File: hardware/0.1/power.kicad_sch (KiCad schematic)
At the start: 31 parts, among them U1 ECP5U_12_CABGA256, U2 TLV73325PDBV, U3 TLV62568DBV, U5 TLV62568DBV

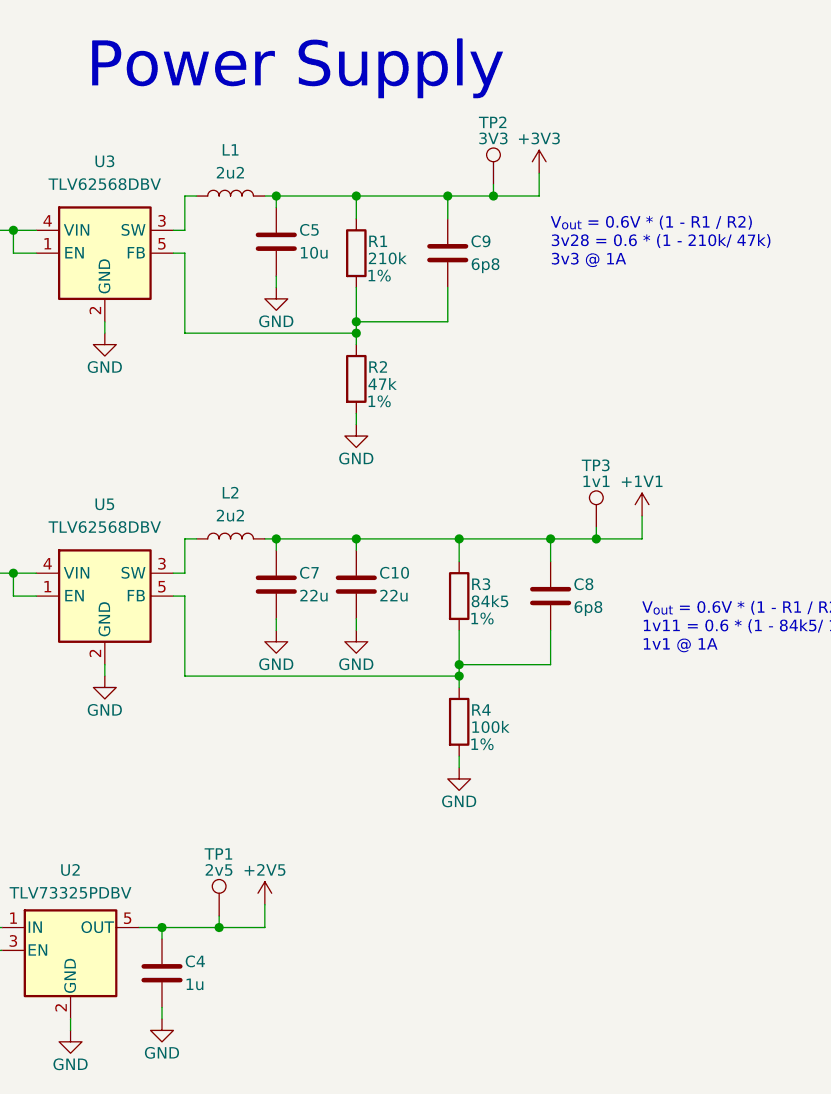
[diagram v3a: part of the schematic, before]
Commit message: hyperram routed
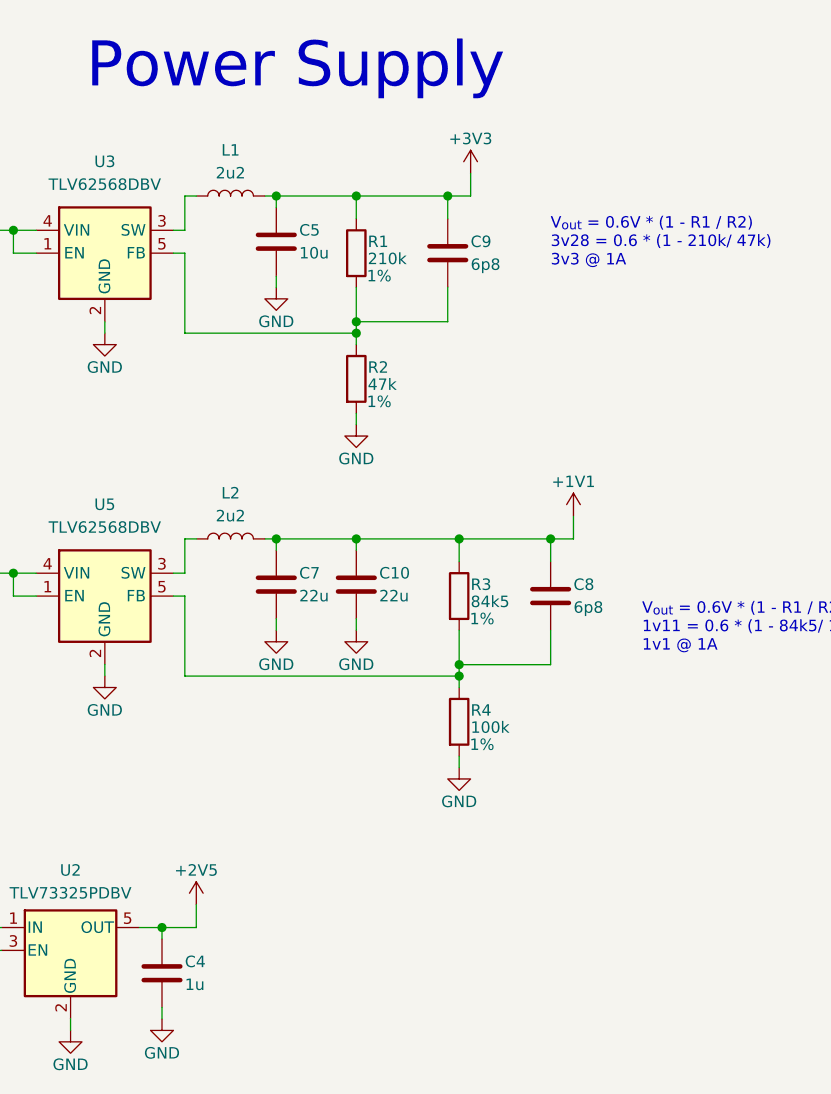
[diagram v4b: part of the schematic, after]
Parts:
- removed TP1: 2v5, TestPoint:TestPoint_Pad_D1.5mm, symbol Connector:TestPoint
- removed TP2: 3V3, TestPoint:TestPoint_Pad_D1.5mm, symbol Connector:TestPoint
- removed TP3: 1v1, TestPoint:TestPoint_Pad_D1.5mm, symbol Connector:TestPoint
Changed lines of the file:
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@@
   (junction (at 34.29 81.28) (diameter 1.016) (color 0 0 0 0))
   (junction (at 50.8 120.65) (diameter 1.016) (color 0 0 0 0))
-  (junction (at 57.15 120.65) (diameter 1.016) (color 0 0 0 0))
   (junction (at 63.5 39.37) (diameter 1.016) (color 0 0 0 0))
   (junction (at 63.5 77.47) (diameter 1.016) (color 0 0 0 0))
@@
   (junction (at 83.82 91.44) (diameter 1.016) (color 0 0 0 0))
   (junction (at 83.82 92.71) (diameter 1.016) (color 0 0 0 0))
-  (junction (at 87.63 39.37) (diameter 1.016) (color 0 0 0 0))
   (junction (at 93.98 77.47) (diameter 1.016) (color 0 0 0 0))
-  (junction (at 99.06 77.47) (diameter 1.016) (color 0 0 0 0))
   (junction (at 182.88 76.2) (diameter 1.016) (color 0 0 0 0))
   (junction (at 182.88 86.36) (diameter 1.016) (color 0 0 0 0))
@@
     (stroke (width 0) (type solid) (color 0 0 0 0))
   )
-  (wire (pts (xy 50.8 120.65) (xy 57.15 120.65))
+  (wire (pts (xy 50.8 120.65) (xy 54.61 120.65))
     (stroke (width 0) (type solid) (color 0 0 0 0))
   )
@@
     (stroke (width 0) (type solid) (color 0 0 0 0))
   )
-  (wire (pts (xy 57.15 119.38) (xy 57.15 120.65))
-    (stroke (width 0) (type solid) (color 0 0 0 0))
-  )
-  (wire (pts (xy 57.15 120.65) (xy 62.23 120.65))
+  (wire (pts (xy 54.61 118.11) (xy 54.61 120.65))
     (stroke (width 0) (type solid) (color 0 0 0 0))
   )
@@
     (stroke (width 0) (type solid) (color 0 0 0 0))
   )
-  (wire (pts (xy 62.23 118.11) (xy 62.23 120.65))
-    (stroke (width 0) (type solid) (color 0 0 0 0))
-  )
   (wire (pts (xy 63.5 39.37) (xy 63.5 40.64))
     (stroke (width 0) (type solid) (color 0 0 0 0))
@@
     (stroke (width 0) (type solid) (color 0 0 0 0))
   )
-  (wire (pts (xy 82.55 39.37) (xy 87.63 39.37))
+  (wire (pts (xy 82.55 39.37) (xy 85.09 39.37))
     (stroke (width 0) (type solid) (color 0 0 0 0))
   )
@@
     (stroke (width 0) (type solid) (color 0 0 0 0))
   )
-  (wire (pts (xy 87.63 38.1) (xy 87.63 39.37))
-    (stroke (width 0) (type solid) (color 0 0 0 0))
-  )
-  (wire (pts (xy 87.63 39.37) (xy 92.71 39.37))
-    (stroke (width 0) (type solid) (color 0 0 0 0))
-  )
-  (wire (pts (xy 92.71 39.37) (xy 92.71 36.83))
+  (wire (pts (xy 85.09 39.37) (xy 85.09 36.83))
     (stroke (width 0) (type solid) (color 0 0 0 0))
   )
@@
     (stroke (width 0) (type solid) (color 0 0 0 0))
   )
-  (wire (pts (xy 93.98 77.47) (xy 99.06 77.47))
+  (wire (pts (xy 93.98 77.47) (xy 96.52 77.47))
     (stroke (width 0) (type solid) (color 0 0 0 0))
   )
@@
     (stroke (width 0) (type solid) (color 0 0 0 0))
   )
-  (wire (pts (xy 99.06 76.2) (xy 99.06 77.47))
-    (stroke (width 0) (type solid) (color 0 0 0 0))
-  )
-  (wire (pts (xy 99.06 77.47) (xy 104.14 77.47))
-    (stroke (width 0) (type solid) (color 0 0 0 0))
-  )
-  (wire (pts (xy 104.14 77.47) (xy 104.14 74.93))
+  (wire (pts (xy 96.52 77.47) (xy 96.52 74.93))
     (stroke (width 0) (type solid) (color 0 0 0 0))
   )
@@
     (effects (font (size 5 5)) (justify right bottom))
   )
-  (symbol (lib_id "Connector:TestPoint") (at 57.15 119.38 0) (unit 1)
-    (in_bom yes) (on_board yes)
-    (property "Reference" "TP1" (id 0) (at 57.15 112.522 0))
-    (property "Value" "2v5" (id 1) (at 57.15 114.3 0))
-    (property "Footprint" "TestPoint:TestPoint_Pad_D1.5mm" (id 2) (at 62.23 119.38 0)
-      (effects (font (size 1.27 1.27)) hide)
-    )
-    (property "Datasheet" "~" (id 3) (at 62.23 119.38 0)
-      (effects (font (size 1.27 1.27)) hide)
-    )
-  )
-  (symbol (lib_id "Connector:TestPoint") (at 87.63 38.1 0) (unit 1)
-    (in_bom yes) (on_board yes)
-    (property "Reference" "TP2" (id 0) (at 87.63 31.242 0))
-    (property "Value" "3V3" (id 1) (at 87.63 33.02 0))
-    (property "Footprint" "TestPoint:TestPoint_Pad_D1.5mm" (id 2) (at 92.71 38.1 0)
-      (effects (font (size 1.27 1.27)) hide)
-    )
-    (property "Datasheet" "~" (id 3) (at 92.71 38.1 0)
-      (effects (font (size 1.27 1.27)) hide)
-    )
-  )
-  (symbol (lib_id "Connector:TestPoint") (at 99.06 76.2 0) (unit 1)
-    (in_bom yes) (on_board yes)
-    (property "Reference" "TP3" (id 0) (at 99.06 69.342 0))
-    (property "Value" "1v1" (id 1) (at 99.06 71.12 0))
-    (property "Footprint" "TestPoint:TestPoint_Pad_D1.5mm" (id 2) (at 104.14 76.2 0)
-      (effects (font (size 1.27 1.27)) hide)
-    )
-    (property "Datasheet" "~" (id 3) (at 104.14 76.2 0)
-      (effects (font (size 1.27 1.27)) hide)
-    )
-  )
   (symbol (lib_id "power:+5V") (at 24.13 118.745 0) (unit 1)
     (in_bom yes) (on_board yes)
@@
     )
   )
-  (symbol (lib_id "power:+2V5") (at 62.23 118.11 0) (unit 1)
-    (in_bom yes) (on_board yes)
-    (property "Reference" "#PWR0112" (id 0) (at 62.23 121.92 0)
-      (effects (font (size 1.27 1.27)) hide)
-    )
-    (property "Value" "+2V5" (id 1) (at 62.23 114.3 0))
-    (property "Footprint" "" (id 2) (at 62.23 118.11 0)
-      (effects (font (size 1.27 1.27)) hide)
-    )
-    (property "Datasheet" "" (id 3) (at 62.23 118.11 0)
-      (effects (font (size 1.27 1.27)) hide)
-    )
-  )
-  (symbol (lib_id "power:+3V3") (at 92.71 36.83 0) (unit 1)
-    (in_bom yes) (on_board yes)
-    (property "Reference" "#PWR0101" (id 0) (at 92.71 40.64 0)
-      (effects (font (size 1.27 1.27)) hide)
-    )
-    (property "Value" "+3V3" (id 1) (at 92.71 33.02 0))
-    (property "Footprint" "" (id 2) (at 92.71 36.83 0)
-      (effects (font (size 1.27 1.27)) hide)
-    )
-    (property "Datasheet" "" (id 3) (at 92.71 36.83 0)
-      (effects (font (size 1.27 1.27)) hide)
-    )
-  )
-  (symbol (lib_id "power:+1V1") (at 104.14 74.93 0) (unit 1)
-    (in_bom yes) (on_board yes)
-    (property "Reference" "#PWR0107" (id 0) (at 104.14 78.74 0)
-      (effects (font (size 1.27 1.27)) hide)
-    )
-    (property "Value" "+1V1" (id 1) (at 104.14 71.12 0))
-    (property "Footprint" "" (id 2) (at 104.14 74.93 0)
-      (effects (font (size 1.27 1.27)) hide)
-    )
-    (property "Datasheet" "" (id 3) (at 104.14 74.93 0)
-      (effects (font (size 1.27 1.27)) hide)
-    )
+  (symbol (lib_id "power:+2V5") (at 54.61 118.11 0) (unit 1)
+    (in_bom yes) (on_board yes)
+    (property "Reference" "#PWR0112" (id 0) (at 54.61 121.92 0)
+      (effects (font (size 1.27 1.27)) hide)
+    )
+    (property "Value" "+2V5" (id 1) (at 54.61 114.3 0))
+    (property "Footprint" "" (id 2) (at 54.61 118.11 0)
+      (effects (font (size 1.27 1.27)) hide)
+    )
+    (property "Datasheet" "" (id 3) (at 54.61 118.11 0)
+      (effects (font (size 1.27 1.27)) hide)
+    )
+  )
+  (symbol (lib_id "power:+3V3") (at 85.09 36.83 0) (unit 1)
+    (in_bom yes) (on_board yes)
+    (property "Reference" "#PWR0101" (id 0) (at 85.09 40.64 0)
+      (effects (font (size 1.27 1.27)) hide)
+    )
+    (property "Value" "+3V3" (id 1) (at 85.09 33.02 0))
+    (property "Footprint" "" (id 2) (at 85.09 36.83 0)
+      (effects (font (size 1.27 1.27)) hide)
+    )
+    (property "Datasheet" "" (id 3) (at 85.09 36.83 0)
+      (effects (font (size 1.27 1.27)) hide)
+    )
+  )
+  (symbol (lib_id "power:+1V1") (at 96.52 74.93 0) (unit 1)
+    (in_bom yes) (on_board yes)
+    (property "Reference" "#PWR0107" (id 0) (at 96.52 78.74 0)
+      (effects (font (size 1.27 1.27)) hide)
+    )
+    (property "Value" "+1V1" (id 1) (at 96.52 71.12 0))
+    (property "Footprint" "" (id 2) (at 96.52 74.93 0)
+      (effects (font (size 1.27 1.27)) hide)
+    )
+    (property "Datasheet" "" (id 3) (at 96.52 74.93 0)
+      (effects (font (size 1.27 1.27)) hide)
+    )

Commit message: all DRC / ERC errors signed off
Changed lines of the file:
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@@
+    (stroke (width 0) (type solid) (color 0 0 0 0))
+  )
+  (wire (pts (xy 142.24 189.23) (xy 142.24 190.5))
+    (stroke (width 0) (type solid) (color 0 0 0 0))
+  )
+  (wire (pts (xy 151.13 190.5) (xy 151.13 189.23))
+    (stroke (width 0) (type solid) (color 0 0 0 0))
+  )
+  (wire (pts (xy 161.29 190.5) (xy 161.29 189.23))
+    (stroke (width 0) (type solid) (color 0 0 0 0))
+  )
+  (wire (pts (xy 171.45 190.5) (xy 171.45 189.23))
     (stroke (width 0) (type solid) (color 0 0 0 0))
   )
@@
     (effects (font (size 5 5)) (justify right bottom))
   )
+  (symbol (lib_id "power:PWR_FLAG") (at 142.24 189.23 0) (unit 1)
+    (in_bom yes) (on_board yes)
+    (property "Reference" "#FLG0102" (id 0) (at 142.24 187.325 0)
+      (effects (font (size 1.27 1.27)) hide)
+    )
+    (property "Value" "PWR_FLAG" (id 1) (at 142.24 185.42 0))
+    (property "Footprint" "" (id 2) (at 142.24 189.23 0)
+      (effects (font (size 1.27 1.27)) hide)
+    )
+    (property "Datasheet" "~" (id 3) (at 142.24 189.23 0)
+      (effects (font (size 1.27 1.27)) hide)
+    )
+  )
+  (symbol (lib_id "power:PWR_FLAG") (at 151.13 190.5 180) (unit 1)
+    (in_bom yes) (on_board yes)
+    (property "Reference" "#FLG0104" (id 0) (at 151.13 192.405 0)
+      (effects (font (size 1.27 1.27)) hide)
+    )
+    (property "Value" "PWR_FLAG" (id 1) (at 151.13 194.31 0))
+    (property "Footprint" "" (id 2) (at 151.13 190.5 0)
+      (effects (font (size 1.27 1.27)) hide)
+    )
+    (property "Datasheet" "~" (id 3) (at 151.13 190.5 0)
+      (effects (font (size 1.27 1.27)) hide)
+    )
+  )
+  (symbol (lib_id "power:PWR_FLAG") (at 161.29 190.5 180) (unit 1)
+    (in_bom yes) (on_board yes)
+    (property "Reference" "#FLG0103" (id 0) (at 161.29 192.405 0)
+      (effects (font (size 1.27 1.27)) hide)
+    )
+    (property "Value" "PWR_FLAG" (id 1) (at 161.29 194.31 0))
+    (property "Footprint" "" (id 2) (at 161.29 190.5 0)
+      (effects (font (size 1.27 1.27)) hide)
+    )
+    (property "Datasheet" "~" (id 3) (at 161.29 190.5 0)
+      (effects (font (size 1.27 1.27)) hide)
+    )
+  )
+  (symbol (lib_id "power:PWR_FLAG") (at 171.45 190.5 180) (unit 1)
+    (in_bom yes) (on_board yes)
+    (property "Reference" "#FLG0101" (id 0) (at 171.45 192.405 0)
+      (effects (font (size 1.27 1.27)) hide)
+    )
+    (property "Value" "PWR_FLAG" (id 1) (at 171.45 194.31 0))
+    (property "Footprint" "" (id 2) (at 171.45 190.5 0)
+      (effects (font (size 1.27 1.27)) hide)
+    )
+    (property "Datasheet" "~" (id 3) (at 171.45 190.5 0)
+      (effects (font (size 1.27 1.27)) hide)
+    )
+  )
   (symbol (lib_id "power:+5V") (at 24.13 118.745 0) (unit 1)
     (in_bom yes) (on_board yes)
@@
     )
     (property "Datasheet" "" (id 3) (at 96.52 74.93 0)
+      (effects (font (size 1.27 1.27)) hide)
+    )
+  )
+  (symbol (lib_id "power:+1V1") (at 151.13 189.23 0) (unit 1)
+    (in_bom yes) (on_board yes)
+    (property "Reference" "#PWR0174" (id 0) (at 151.13 193.04 0)
+      (effects (font (size 1.27 1.27)) hide)
+    )
+    (property "Value" "+1V1" (id 1) (at 151.13 185.42 0))
+    (property "Footprint" "" (id 2) (at 151.13 189.23 0)
+      (effects (font (size 1.27 1.27)) hide)
+    )
+    (property "Datasheet" "" (id 3) (at 151.13 189.23 0)
+      (effects (font (size 1.27 1.27)) hide)
+    )
+  )
+  (symbol (lib_id "power:+3V3") (at 161.29 189.23 0) (mirror y) (unit 1)
+    (in_bom yes) (on_board yes)
+    (property "Reference" "#PWR0173" (id 0) (at 161.29 193.04 0)
+      (effects (font (size 1.27 1.27)) hide)
+    )
+    (property "Value" "+3V3" (id 1) (at 161.29 185.42 0))
+    (property "Footprint" "" (id 2) (at 161.29 189.23 0)
+      (effects (font (size 1.27 1.27)) hide)
+    )
+    (property "Datasheet" "" (id 3) (at 161.29 189.23 0)
+      (effects (font (size 1.27 1.27)) hide)
+    )
+  )
+  (symbol (lib_id "power:+5V") (at 171.45 189.23 0) (unit 1)
+    (in_bom yes) (on_board yes)
+    (property "Reference" "#PWR0171" (id 0) (at 171.45 193.04 0)
+      (effects (font (size 1.27 1.27)) hide)
+    )
+    (property "Value" "+5V" (id 1) (at 171.45 185.42 0))
+    (property "Footprint" "" (id 2) (at 171.45 189.23 0)
+      (effects (font (size 1.27 1.27)) hide)
+    )
+    (property "Datasheet" "" (id 3) (at 171.45 189.23 0)
       (effects (font (size 1.27 1.27)) hide)
     )
@@
       (effects (font (size 1.27 1.27)) hide)
     )
+  )
+  (symbol (lib_id "power:GND") (at 142.24 190.5 0) (unit 1)
+    (in_bom yes) (on_board yes)
+    (property "Reference" "#PWR0172" (id 0) (at 142.24 196.85 0)
+      (effects (font (size 1.27 1.27)) hide)
+    )
+    (property "Value" "GND" (id 1) (at 142.24 194.31 0))
+    (property "Footprint" "" (id 2) (at 142.24 190.5 0)
+      (effects (font (size 1.27 1.27)) hide)
+    )
+    (property "Datasheet" "" (id 3) (at 142.24 190.5 0)
+      (effects (font (size 1.27 1.27)) hide)
+    )

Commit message: adding silk
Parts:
- U1: manf# ECP5U_12 -> (none)
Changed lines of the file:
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@@
       (effects (font (size 1.27 1.27) italic) hide)
     )
-    (property "Datasheet" "http://www.ti.com/lit/ds/symlink/tlv733p.pdf" (id 3) (at 40.64 123.19 0)
+    (property "Datasheet" "" (id 3) (at 40.64 123.19 0)
       (effects (font (size 1.27 1.27)) hide)
     )
@@
       (effects (font (size 1.27 1.27) italic) (justify left) hide)
     )
-    (property "Datasheet" "http://www.ti.com/lit/ds/symlink/tlv62568.pdf" (id 3) (at 38.1 34.29 0)
+    (property "Datasheet" "" (id 3) (at 38.1 34.29 0)
       (effects (font (size 1.27 1.27)) hide)
     )
@@
       (effects (font (size 1.27 1.27) italic) (justify left) hide)
     )
-    (property "Datasheet" "http://www.ti.com/lit/ds/symlink/tlv62568.pdf" (id 3) (at 38.1 72.39 0)
+    (property "Datasheet" "" (id 3) (at 38.1 72.39 0)
       (effects (font (size 1.27 1.27)) hide)
     )
@@
       (effects (font (size 1.524 1.524)) (justify right) hide)
     )
-    (property "manf#" "ECP5U_12" (id 4) (at 223.52 2.54 0)
+    (property "manf#" "" (id 4) (at 223.52 2.54 0)
       (effects (font (size 1.524 1.524)) (justify right) hide)
     )

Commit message: change LEDs, optimise parts
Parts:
- C10, C7: LCSC (none) -> C100082; MPN (none) -> CL10B225KP8NNNC
- L1, L2: LCSC (none) -> C216156; MPN (none) -> SLM20122R2MIT
- R1: MPN (none) -> 0402WGF2103TCE
- R2: MPN (none) -> RC0402FR-0747KL
- R3: MPN (none) -> 0402WGF8452TCE
- R4: MPN (none) -> 0402WGF1003TCE
- U3, U5: LCSC (none) -> C163219; MPN (none) -> TLV62568DBVR
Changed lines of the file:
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@@
+      (effects (font (size 1.27 1.27)) hide)
+    )
+    (property "LCSC" "C216156" (id 4) (at 58.42 39.37 0)
+      (effects (font (size 1.27 1.27)) hide)
+    )
+    (property "MPN" "SLM20122R2MIT" (id 5) (at 58.42 39.37 0)
       (effects (font (size 1.27 1.27)) hide)
     )
@@
       (effects (font (size 1.27 1.27)) hide)
     )
+    (property "LCSC" "C216156" (id 4) (at 58.42 77.47 0)
+      (effects (font (size 1.27 1.27)) hide)
+    )
+    (property "MPN" "SLM20122R2MIT" (id 5) (at 58.42 77.47 0)
+      (effects (font (size 1.27 1.27)) hide)
+    )
   )
   (symbol (lib_id "power:GND") (at 26.67 54.61 0) (unit 1)
@@
     )
     (property "Tolerance" "1%" (id 4) (at 74.93 48.26 0))
+    (property "MPN" "0402WGF2103TCE" (id 5) (at 72.39 45.72 0)
+      (effects (font (size 1.27 1.27)) hide)
+    )
   )
   (symbol (lib_id "Device:R") (at 72.39 59.69 0) (unit 1)
@@
     )
     (property "Tolerance" "1%" (id 4) (at 74.93 62.23 0))
+    (property "MPN" "RC0402FR-0747KL" (id 5) (at 72.39 59.69 0)
+      (effects (font (size 1.27 1.27)) hide)
+    )
   )
   (symbol (lib_id "Device:R") (at 83.82 83.82 0) (unit 1)
@@
     )
     (property "Tolerance" "1%" (id 4) (at 86.36 86.36 0))
+    (property "MPN" "0402WGF8452TCE" (id 5) (at 83.82 83.82 0)
+      (effects (font (size 1.27 1.27)) hide)
+    )
   )
   (symbol (lib_id "Device:R") (at 83.82 97.79 0) (unit 1)
@@
     )
     (property "Tolerance" "1%" (id 4) (at 86.36 100.33 0))
+    (property "MPN" "0402WGF1003TCE" (id 5) (at 83.82 97.79 0)
+      (effects (font (size 1.27 1.27)) hide)
+    )
   )
   (symbol (lib_id "Device:C") (at 26.67 48.26 0) (unit 1)
@@
       (effects (font (size 1.27 1.27)) hide)
     )
+    (property "LCSC" "C100082" (id 4) (at 63.5 82.55 0)
+      (effects (font (size 1.27 1.27)) hide)
+    )
+    (property "MPN" "CL10B225KP8NNNC" (id 5) (at 63.5 82.55 0)
+      (effects (font (size 1.27 1.27)) hide)
+    )
   )
   (symbol (lib_id "Device:C") (at 72.39 82.55 0) (unit 1)
@@
     )
     (property "Datasheet" "~" (id 3) (at 72.39 82.55 0)
+      (effects (font (size 1.27 1.27)) hide)
+    )
+    (property "LCSC" "C100082" (id 4) (at 72.39 82.55 0)
+      (effects (font (size 1.27 1.27)) hide)
+    )
+    (property "MPN" "CL10B225KP8NNNC" (id 5) (at 72.39 82.55 0)
       (effects (font (size 1.27 1.27)) hide)
     )
@@
       (effects (font (size 1.27 1.27)) hide)
     )
+    (property "LCSC" "C163219" (id 4) (at 44.45 45.72 0)
+      (effects (font (size 1.27 1.27)) hide)
+    )
+    (property "MPN" "TLV62568DBVR" (id 5) (at 44.45 45.72 0)
+      (effects (font (size 1.27 1.27)) hide)
+    )
   )
   (symbol (lib_id "Regulator_Switching:TLV62568DBV") (at 44.45 83.82 0) (unit 1)
@@
       (effects (font (size 1.27 1.27)) hide)
     )
+    (property "LCSC" "C163219" (id 4) (at 44.45 83.82 0)
+      (effects (font (size 1.27 1.27)) hide)
+    )
+    (property "MPN" "TLV62568DBVR" (id 5) (at 44.45 83.82 0)
+      (effects (font (size 1.27 1.27)) hide)
+    )
